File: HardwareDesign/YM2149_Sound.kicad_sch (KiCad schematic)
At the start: 1 part, among them U801 YM2149

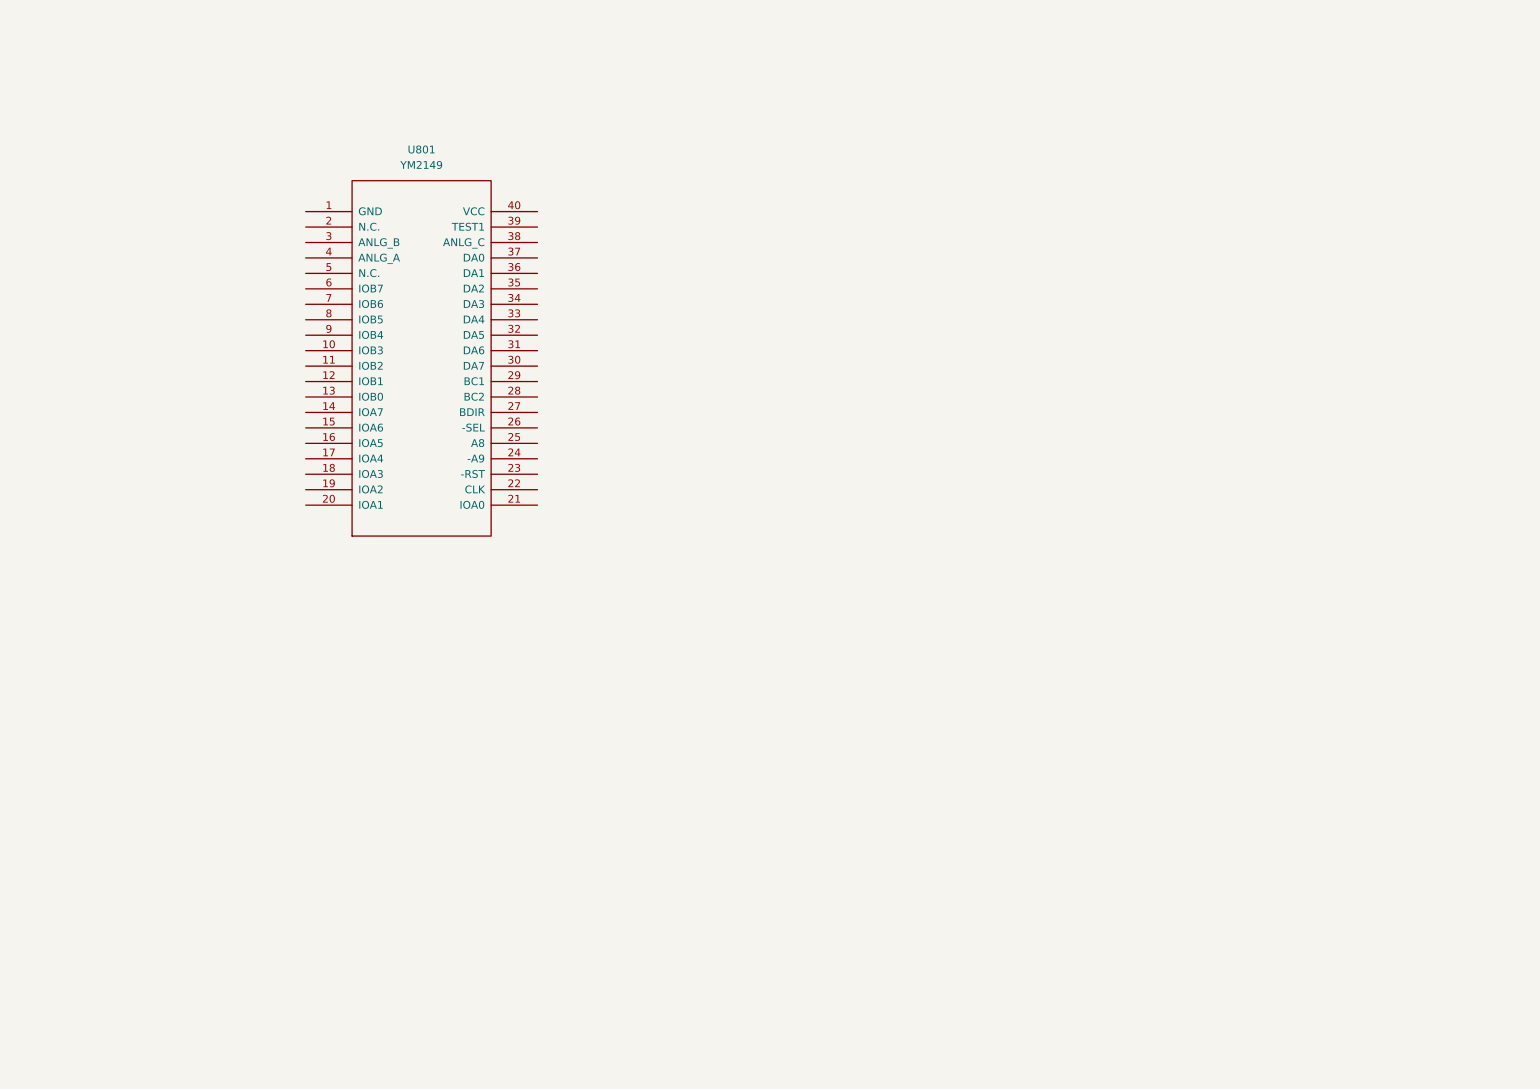
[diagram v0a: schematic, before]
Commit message: generate bus signals for YM2149
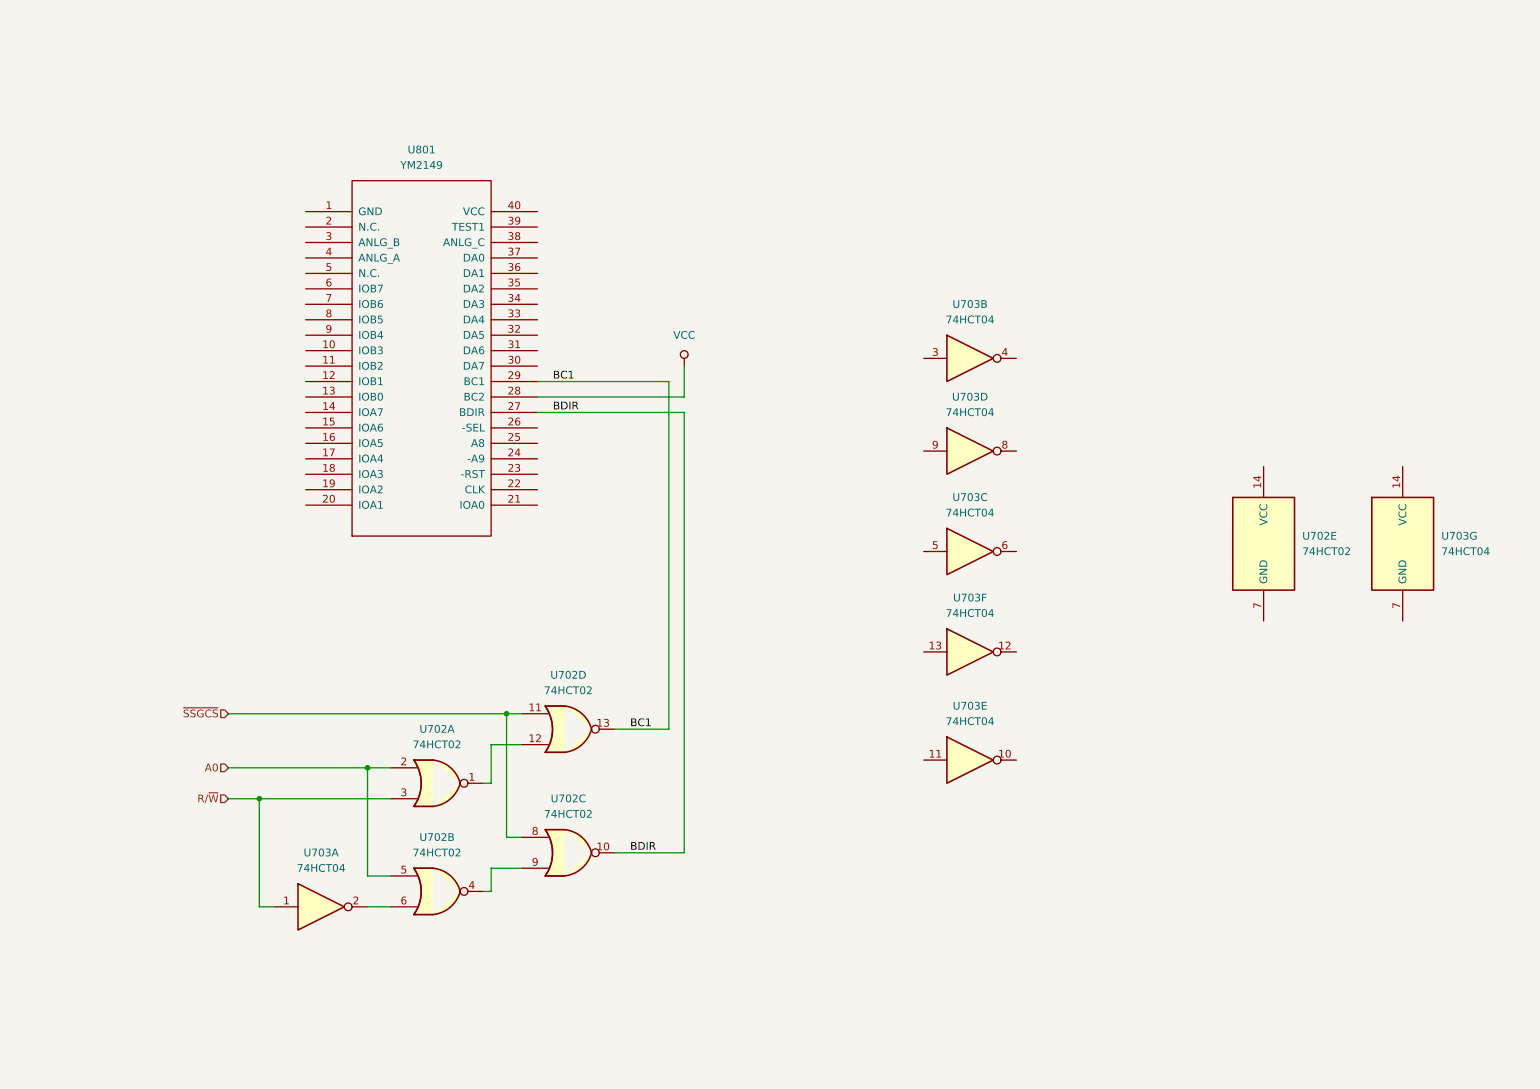
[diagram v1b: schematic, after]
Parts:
- added U702: 74HCT02, symbol 74xx:74HCT02
- added U703: 74HCT04, symbol 74xx:74HCT04
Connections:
- net BDIR: now reaches U801.27 (BDIR)
- net BDIR: now also U702.10
- net VCC: now reaches U801.28 (BC2)
- net BC1: now reaches U801.29 (BC1)
- net BC1: now also U702.13
- new net: U702.4, U702.9
- new net: U702.6, U703.2
- new net: U702.1, U702.12
- new net A0: U702.2, U702.5
- new net R/~{W}: U702.3, U703.1
- new net ~{SSGCS}: U702.11, U702.8

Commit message: more work on YM2149 module
Also, rearranged top-level schematic a bit.
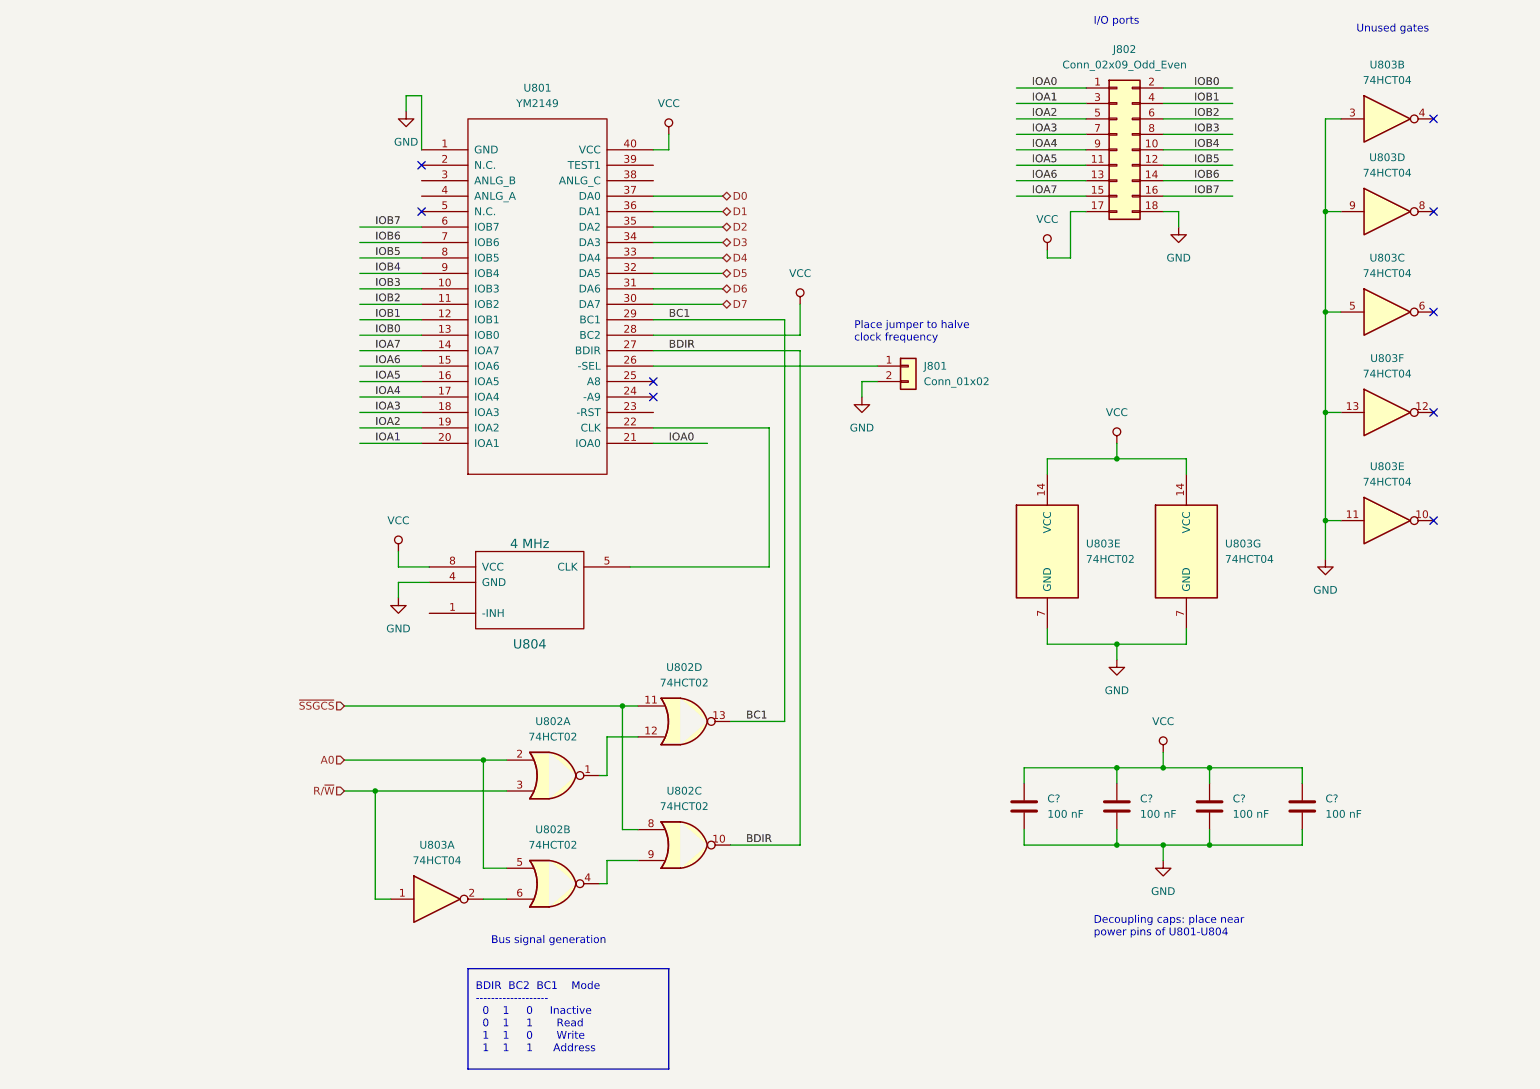
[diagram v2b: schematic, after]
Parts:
- added C? (x4): 100 nF, symbol device:C
- added J801: Conn_01x02, symbol Connector_Generic:Conn_01x02
- added J802: Conn_02x09_Odd_Even, symbol Connector_Generic:Conn_02x09_Odd_Even
- added U804: 4 MHz, symbol ya68k:XTAL_OSC_HALF_CAN
- renumbered U702 to U802, U703 to U803, U702 to U803
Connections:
- net VCC: now also U801.40 (VCC), U803.14 (VCC), U803.14 (VCC), C?.1, C?.1, C?.1, C?.1, J802.17 (Pin_17), U804.8 (VCC)
- net GND: now reaches U803.5
- net GND: now also U801.1 (GND), U803.11, U803.13, U803.3, U803.7 (GND), U803.7 (GND), U803.9, C?.2, C?.2, C?.2, C?.2, J801.2 (Pin_2), J802.18 (Pin_18), U804.4 (GND)
- net IOB3: now reaches U801.10 (IOB3)
- net IOB3: now also J802.8 (Pin_8)
- net IOB2: now reaches U801.11 (IOB2)
- net IOB2: now also J802.6 (Pin_6)
- net IOB1: now reaches U801.12 (IOB1)
- net IOB1: now also J802.4 (Pin_4)
- net IOB0: now reaches U801.13 (IOB0)
- net IOB0: now also J802.2 (Pin_2)
- net IOA7: now reaches U801.14 (IOA7)
- net IOA7: now also J802.15 (Pin_15)
- net IOA6: now reaches U801.15 (IOA6)
- net IOA6: now also J802.13 (Pin_13)
- net IOA5: now reaches U801.16 (IOA5)
- net IOA5: now also J802.11 (Pin_11)
- net IOA4: now reaches U801.17 (IOA4)
- net IOA4: now also J802.9 (Pin_9)
- net IOA3: now reaches U801.18 (IOA3)
- net IOA3: now also J802.7 (Pin_7)
- net IOA2: now reaches U801.19 (IOA2)
- net IOA2: now also J802.5 (Pin_5)
- net IOA1: now reaches U801.20 (IOA1)
- net IOA1: now also J802.3 (Pin_3)
- net IOA0: now reaches U801.21 (IOA0)
- net IOA0: now also J802.1 (Pin_1)
- net at U801.22 (CLK): now also U804.5 (CLK)
- net at U801.26 (-SEL): now also J801.1 (Pin_1)
- net D7: now reaches U801.30 (DA7)
- net D6: now reaches U801.31 (DA6)
- net D5: now reaches U801.32 (DA5)
- net D4: now reaches U801.33 (DA4)
- net D3: now reaches U801.34 (DA3)
- net D2: now reaches U801.35 (DA2)
- net D1: now reaches U801.36 (DA1)
- net D0: now reaches U801.37 (DA0)
- net IOB7: now reaches U801.6 (IOB7)
- net IOB7: now also J802.16 (Pin_16)
- net IOB6: now reaches U801.7 (IOB6)
- net IOB6: now also J802.14 (Pin_14)
- net IOB5: now reaches U801.8 (IOB5)
- net IOB5: now also J802.12 (Pin_12)
- net IOB4: now reaches U801.9 (IOB4)
- net IOB4: now also J802.10 (Pin_10)
- no-connect marks 0 -> 9
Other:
- note added: "BDIR BC2 BC1 Mode ------------------- 0 1 0 Inactive 0 1 1 Read 1 1 0 Write 1 1 1 Address"
- note added: "Bus signal generation"
- note added: "Decoupling caps: place near power pins of U801-U804"
- note added: "I/O ports"
- note added: "Place jumper to halve clock frequency"
- note added: "Unused gates"
- company: (none) -> daveho hacks
- title: (none) -> YM2149 sound module
- moved on the sheet: U801, U802A, U802B, U802C, U802D, U803A, U803B, U803C, U803D, U803E, U803F, U803G

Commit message: YM2149 circuit ready for prototyping?
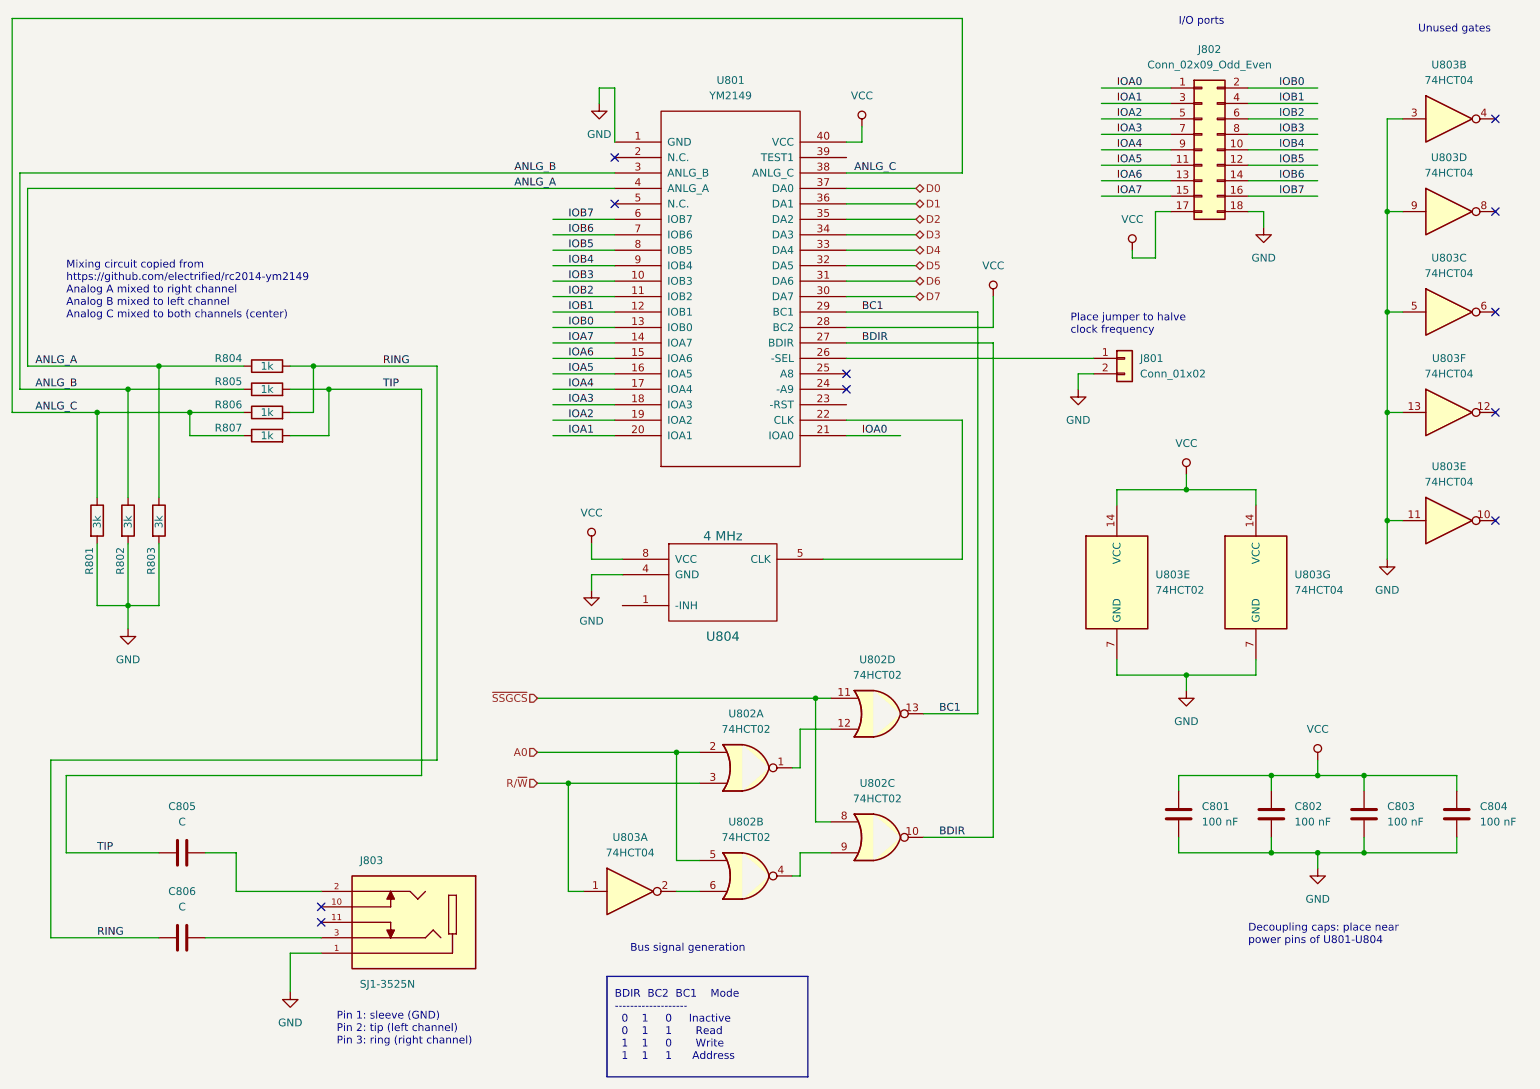
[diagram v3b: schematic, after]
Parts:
- added C805, C806: C, symbol device:C
- added J803: SJ1-3525N, CUI_SJ1-3525N, symbol SJ1-3525N:SJ1-3525N
- added R801, R802, R803: 3k, symbol Device:R
- added R804, R805, R806, R807: 1k, symbol device:R
- gave numbers to parts that had none: 4
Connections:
- net GND: now also J803.1, R801.2, R802.2, R803.2
- net ANLG_B: now reaches U801.3 (ANLG_B)
- net ANLG_B: now also R802.1, R805.1
- net ANLG_C: now reaches U801.38 (ANLG_C)
- net ANLG_C: now also R801.1, R806.1, R807.1
- net ANLG_A: now reaches U801.4 (ANLG_A)
- net ANLG_A: now also R803.1, R804.1
- new net: C805.2, J803.2
- new net: C806.2, J803.3
- new net RING: C806.1, R804.2, R806.2
- new net TIP: C805.1, R805.2, R807.2
- no-connect marks 9 -> 11
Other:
- note added: "Mixing circuit copied from https://github.com/electrified/rc2014-ym2149 Analog A mixed to right channel Analog B mixed to left channel Analog C mixed to both channels (center)"
- note added: "Pin 1: sleeve (GND) Pin 2: tip (left channel) Pin 3: ring (right channel)"
- moved on the sheet: C801, C802, C803, C804, J801, J802, U801, U802A, U802B, U802C, U802D, U803A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
